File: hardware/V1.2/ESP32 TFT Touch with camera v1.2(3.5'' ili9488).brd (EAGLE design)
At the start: 66.1 x 84.3 mm, 100 parts, among them IC1 CP2104, P2 AFC01-S06FCC-00, P3 AFC01-S06FCC-00, P5 FPC-40P, Q2 AO3400, Q3 S8050, Q4 S8050, Q5 S8050, U2 ESP32-WROVER, U4 LD1117/3.3v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

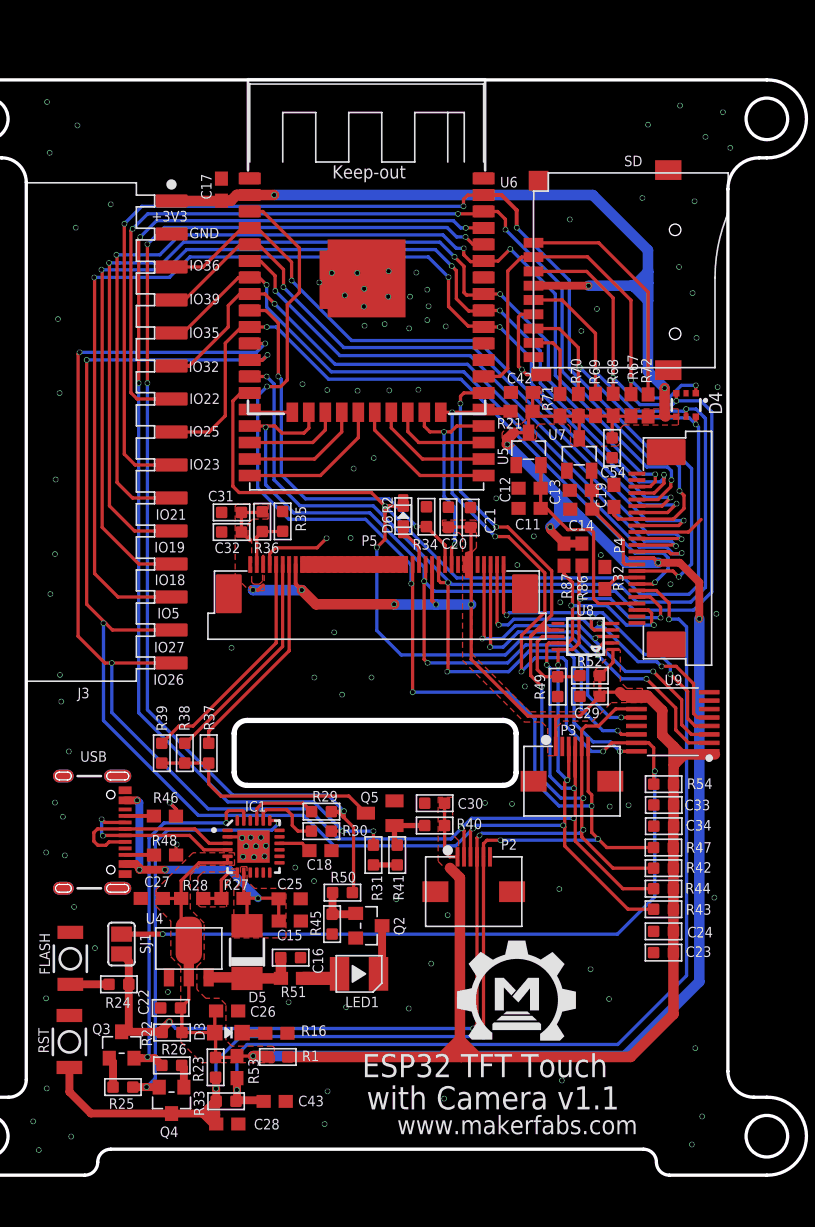
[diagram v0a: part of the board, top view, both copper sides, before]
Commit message: change SCH to V1.2
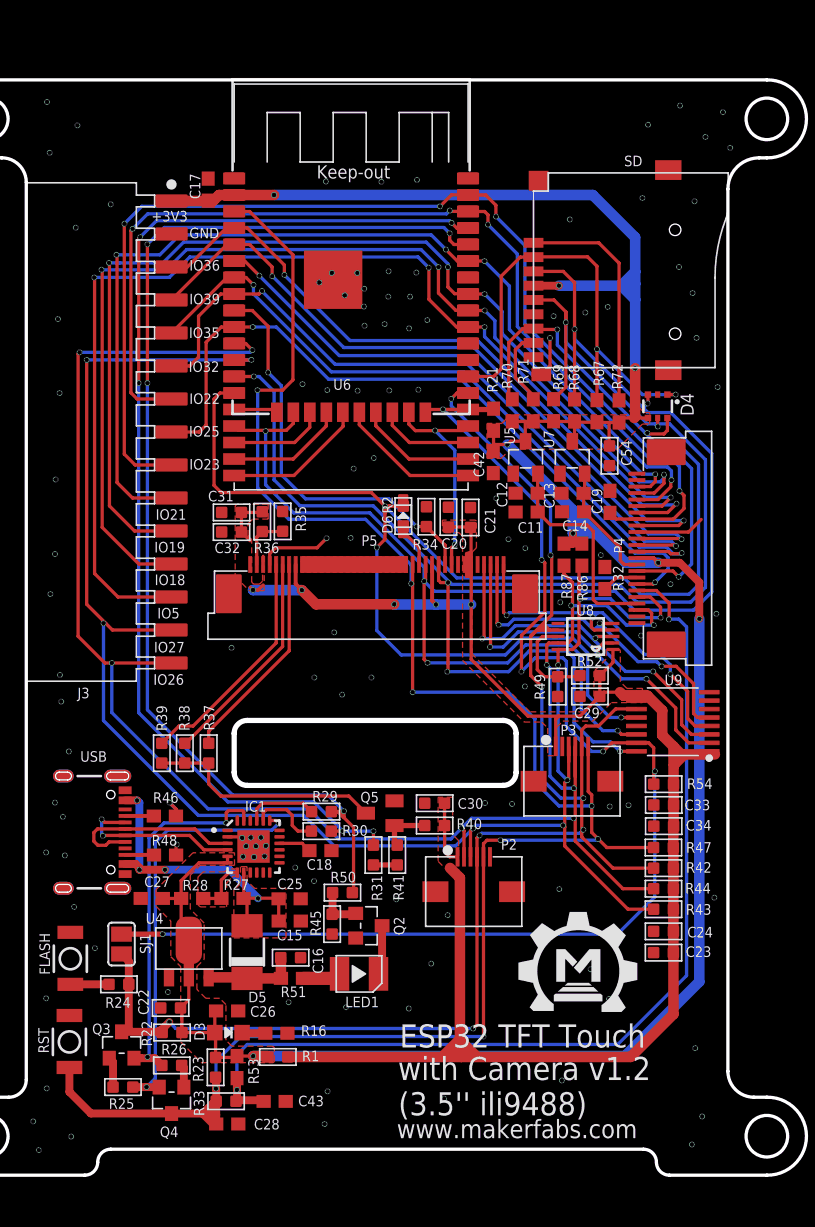
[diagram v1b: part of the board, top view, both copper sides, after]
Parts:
- U6: device esp32:ESP-WROOM-32 -> ESP32:ESP-WROOM-32
- moved C42 5.79 mm to (35.9, 54.9), turned to 270 degrees
- moved U$1 5.22 mm to (38.4, 12.6)
- moved R70 5.10 mm to (37.4, 58.9)
- moved R69 3.25 mm to (40.6, 58.9)
- moved R68 3.00 mm to (42.2, 58.9)
- moved R67 2.66 mm to (43.9, 58.8)
- moved R72 2.28 mm to (45.6, 58.8)
- moved R21 2.25 mm to (36.0, 58.1), turned to 90 degrees
- moved D4 2.19 mm to (48.6, 59.2)
- moved R71 2.10 mm to (39.0, 58.9)
- moved U2 1.20 mm to (16.0, 52.6)
- moved U6 1.19 mm to (25.0, 69.0)
- moved C17 1.02 mm to (14.0, 75.8)
- moved U5 0.70 mm to (38.4, 55.2)
- moved C13 0.67 mm to (42.0, 52.5)
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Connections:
- net GND: no longer U6.GND
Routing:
- net +3V3: track 213.4 -> 206.4 mm
- net IO12/HMISO: track 117.7 -> 124.6 mm
- net IO14/HSCLK: track 111.8 -> 116.0 mm
- net GND: track 76.5 -> 72.5 mm, vias 113 -> 115
- net CSI_D3: track 82.2 -> 79.3 mm
- net IO4: track 34.8 -> 36.7 mm
- net IO2/SPI_NCS2: track 101.6 -> 103.3 mm
- net TWI_SCK: track 137.9 -> 136.3 mm
- net CSI_HSYNC: track 92.5 -> 91.2 mm
- net TXD: track 87.7 -> 86.5 mm
- net CSI_MCLK: track 53.2 -> 54.3 mm
- net CSI_D2: track 79.5 -> 78.6 mm
- net RXD: track 90.6 -> 89.7 mm
- net IO13/HMOSI: track 117.6 -> 118.5 mm
- net IO0/LCD_IRQ: track 121.0 -> 120.2 mm
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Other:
- board text added: "(3.5'' ili9488)"
- board text added: "with Camera v1.2"
- board text removed: "with Camera v1.1"
